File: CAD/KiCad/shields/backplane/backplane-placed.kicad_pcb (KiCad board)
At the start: 2 copper layers, 210 x 297 mm, 103 parts, among them J1 DSUB-15, J2 DC jack, J5 DSUB-15, J6 screw bridge, J7 JST EH 3, M1 U2D2

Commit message: Route the shield set and validate shared interfaces
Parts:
- added HM1: M3 computing shield, Shields:MountingHole_3.2mm_M3, F.Cu at (143.7, 149.8)
- added HM2: M3 computing shield, Shields:MountingHole_3.2mm_M3, F.Cu at (192.0, 68.6)
- added HM3: M3 computing shield, Shields:MountingHole_3.2mm_M3, F.Cu at (192.0, 143.5)
- added HM4: M3 computing shield, Shields:MountingHole_3.2mm_M3, F.Cu at (143.7, 67.3)

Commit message: Remove shield identification and adopt the simplified connector and Teensy pin maps
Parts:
- removed CI1: 10uF X7R, Shields:C_0805_2012Metric
- removed H1, H2, H3, H4: M3 3.2mm NPTH, Colloquy:MountingHole_3.2mm_M3
- removed RI1, RI2: 4K7, Shields:R_0603_1608Metric
- removed TPI2: shield/sda, Shields:TestPoint_Pad_D1.5mm
- removed TPI3: shield/scl, Shields:TestPoint_Pad_D1.5mm
- added TPA1: female1/analyser out, Shields:TestPoint_Pad_D1.5mm, F.Cu at (100.0, 305.0)
- added TPA2: female2/analyser out, Shields:TestPoint_Pad_D1.5mm, F.Cu at (122.0, 305.0)
- added TPA3: female3/analyser out, Shields:TestPoint_Pad_D1.5mm, F.Cu at (144.0, 305.0)
- added TPA4: male1/analyser out, Shields:TestPoint_Pad_D1.5mm, F.Cu at (166.0, 305.0)
- added TPA5: male2/analyser out, Shields:TestPoint_Pad_D1.5mm, F.Cu at (188.0, 305.0)
- added TPL1: female1/filter out, Shields:TestPoint_Pad_D1.5mm, F.Cu at (90.0, 225.0)
- added TPL2: female2/filter out, Shields:TestPoint_Pad_D1.5mm, F.Cu at (122.0, 225.0)
- added TPL3: female3/filter out, Shields:TestPoint_Pad_D1.5mm, F.Cu at (154.0, 225.0)
- added TPL4: male1/filter out, Shields:TestPoint_Pad_D1.5mm, F.Cu at (186.0, 225.0)
- added TPL5: male2/filter out, Shields:TestPoint_Pad_D1.5mm, F.Cu at (218.0, 225.0)
- added TPM1: female1/microphone, Shields:TestPoint_Pad_D1.5mm, F.Cu at (100.0, 283.0)
- added TPM2: female2/microphone, Shields:TestPoint_Pad_D1.5mm, F.Cu at (122.0, 283.0)
- added TPM3: female3/microphone, Shields:TestPoint_Pad_D1.5mm, F.Cu at (144.0, 283.0)
- added TPM4: male1/microphone, Shields:TestPoint_Pad_D1.5mm, F.Cu at (166.0, 283.0)
- added TPM5: male2/microphone, Shields:TestPoint_Pad_D1.5mm, F.Cu at (188.0, 283.0)
- JA1: value ANALYSER - KEY 24 -> ANALYSER - KEY 22; footprint Shields:Header_2x12_Key24 -> Shields:Header_2x11_Key22
- JV1: value female1 - KEY 14 -> female1 - KEY 6; footprint Shields:Header_2x07_Key14 -> Shields:Header_2x03_Key6
- JV2: value female2 - KEY 14 -> female2 - KEY 6; footprint Shields:Header_2x07_Key14 -> Shields:Header_2x03_Key6
- JV3: value female3 - KEY 14 -> female3 - KEY 6; footprint Shields:Header_2x07_Key14 -> Shields:Header_2x03_Key6
- JV4: value male1 - KEY 14 -> male1 - KEY 6; footprint Shields:Header_2x07_Key14 -> Shields:Header_2x03_Key6
- JV5: value male2 - KEY 14 -> male2 - KEY 6; footprint Shields:Header_2x07_Key14 -> Shields:Header_2x03_Key6
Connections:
- A1 pad SCL: shield/scl -> (no net)
- A1 pad SDA: shield/sda -> (no net)
- JA1 pad 19: shield/sda -> IOREF
- JA1 pad 20: shield/scl -> GND
- JA1 pad 21: IOREF -> +5V

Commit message: Route microphones directly to Teensy and remove the analyser buffer board
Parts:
- removed TPI1: IOREF, Shields:TestPoint_Pad_D1.5mm
- added RM1: 4K7, Shields:R_0603_1608Metric, F.Cu at (100.0, 289.0)
- added RM2: 4K7, Shields:R_0603_1608Metric, F.Cu at (122.0, 289.0)
- added RM3: 4K7, Shields:R_0603_1608Metric, F.Cu at (144.0, 289.0)
- added RM4: 4K7, Shields:R_0603_1608Metric, F.Cu at (166.0, 289.0)
- added RM5: 4K7, Shields:R_0603_1608Metric, F.Cu at (184.0, 289.0)
- added RMD1: 1M, Shields:R_0603_1608Metric, F.Cu at (104.0, 292.0)
- added RMD2: 1M, Shields:R_0603_1608Metric, F.Cu at (126.0, 292.0)
- added RMD3: 1M, Shields:R_0603_1608Metric, F.Cu at (148.0, 292.0)
- added RMD4: 1M, Shields:R_0603_1608Metric, F.Cu at (170.0, 292.0)
- added RMD5: 1M, Shields:R_0603_1608Metric, F.Cu at (184.0, 293.0)
- added TPD1: female1/mic direct, Shields:TestPoint_Pad_D1.5mm, F.Cu at (100.0, 296.0)
- added TPD2: female2/mic direct, Shields:TestPoint_Pad_D1.5mm, F.Cu at (122.0, 296.0)
- added TPD3: female3/mic direct, Shields:TestPoint_Pad_D1.5mm, F.Cu at (144.0, 296.0)
- added TPD4: male1/mic direct, Shields:TestPoint_Pad_D1.5mm, F.Cu at (166.0, 296.0)
- added TPD5: male2/mic direct, Shields:TestPoint_Pad_D1.5mm, F.Cu at (184.0, 298.0)
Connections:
- A1 pad D26: (no net) -> female1/mic direct
- A1 pad D27: (no net) -> female2/mic direct
- A1 pad D28: (no net) -> female3/mic direct
- A1 pad D29: (no net) -> male1/mic direct
- A1 pad D30: (no net) -> male2/mic direct
- A1 pad IORF: IOREF -> (no net)
- JA1 pad 19: IOREF -> MEGA_5V
- JA1 pad 21: +5V -> GND
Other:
- copper layers 2 -> 4
- board text added: "1"
- board text added: "1 ANA"
- board text added: "1 LINE"
- board text added: "2 ANA"
- board text added: "2 LINE"
- board text added: "3 ANA"
- board text added: "3 LINE"
- board text added: "4 ANA"
- board text added: "4 LINE"
- board text added: "5 ANA"
- board text added: "5 LINE"
- board text added: "AGND"
- board text added: "AMP SHUTDOWN"
- board text added: "ANA 1"
- board text added: "ANA 2"
- board text added: "ANA 3"
- board text added: "ANA 4"
- board text added: "ANA 5"
- board text added: "AUDIO RTN"
- board text added: "BOARD +5V"
- board text added: "CARD PITCH Hz"
- board text added: "CHANGE A SHIELD ONLY WITH BOTH UNPLUGGED"
- board text added: "COLLOQUY - SHIELD BACKPLANE - REV A"
- board text added: "COMPUTING SLOT MEGA 2560 OR TEENSY ADAPTER"
- board text added: "GND"
- board text added: "JA1 - MSGEQ7 ANALYSER - MEGA ONLY - EMPTY WITH TEENSY"
- board text added: "JP1 - ONLY AGND-GND BOND"
- board text added: "JV1 - FEMALE1 MEGA D6 - TEENSY 2"
- board text added: "JV2 - FEMALE2 MEGA D46 - TEENSY 4"
- board text added: "JV3 - FEMALE3 MEGA D10 - TEENSY 5"
- board text added: "JV4 - MALE1 MEGA D11 - TEENSY 6"
- board text added: "JV5 - MALE2 MEGA D5 - TEENSY 28"
- board text added: "KEY <-"
- board text added: "LINE 1"
- board text added: "LINE 2"
- board text added: "LINE 3"
- board text added: "LINE 4"
- board text added: "LINE 5"
- board text added: "LINE OUT"
- board text added: "M3"
- board text added: "MEGA 5V (COMPUTING USB)"
- board text added: "MIC 1"
- board text added: "MIC 2"
- board text added: "MIC 3"
- board text added: "MIC 4"
- board text added: "MIC 5"
- board text added: "MIC DIRECT - 4.7 K - TO TEENSY A0-A4"
- board text added: "MIC DIRECT 1"
- board text added: "MIC DIRECT 2"
- board text added: "MIC DIRECT 3"
- board text added: "MIC DIRECT 4"
- board text added: "MIC DIRECT 5"
- board text added: "MIC ORDER F1 F2 F3 M1 M2 - MODULE N = BODY N"
- board text added: "POWER RACK AND COMPUTING USB TOGETHER"
- board text added: "RESET"
- board text added: "SERVO BUS - 12 V"
- board text added: "SLOT N = BODY N"
- board text added: "STROBE"
- board text added: "TONE 1"
- board text added: "TONE 2"
- board text added: "TONE 3"
- board text added: "TONE 4"
- board text added: "TONE 5"
- board text added: "U2D2"
- board text added: "USB END ^"
- board text removed: "COLLOQUY / SHIELDS / A"
- board text removed: "IOREF: MEGA 5V / TEENSY 3.3V"
- board text removed: "JV1 female1"
- board text removed: "JV2 female2"
- board text removed: "JV3 female3"
- board text removed: "JV4 male1"
- board text removed: "JV5 male2"

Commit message: Update shields for Thomas RC cards, debug headers and body microphones
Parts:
- removed TP11, TP12, TP13, TP14, TP15: test pad, Shields:TestPoint_Pad_D1.5mm
- added DP12: GREEN LED, Shields:LED_0603_1608Metric, F.Cu at (217.0, 84.0)
- added DP5: GREEN LED, Shields:LED_0603_1608Metric, F.Cu at (210.0, 84.0)
- added DPUSB: GREEN LED, Shields:LED_0603_1608Metric, F.Cu at (224.0, 84.0)
- added DT1: YELLOW LED, Shields:LED_0603_1608Metric, F.Cu at (82.5, 194.0)
- added DT2: YELLOW LED, Shields:LED_0603_1608Metric, F.Cu at (113.0, 194.0)
- added DT3: YELLOW LED, Shields:LED_0603_1608Metric, F.Cu at (143.5, 194.0)
- added DT4: YELLOW LED, Shields:LED_0603_1608Metric, F.Cu at (174.0, 194.0)
- added DT5: YELLOW LED, Shields:LED_0603_1608Metric, F.Cu at (204.5, 194.0)
- added RLP12: 4K7, Shields:R_0603_1608Metric, F.Cu at (217.0, 87.0)
- added RLP5: 2K2, Shields:R_0603_1608Metric, F.Cu at (210.0, 87.0)
- added RLPUSB: 2K2, Shields:R_0603_1608Metric, F.Cu at (224.0, 87.0)
- added RLT1: 1K5, Shields:R_0603_1608Metric, F.Cu at (82.5, 197.0)
- added RLT2: 1K5, Shields:R_0603_1608Metric, F.Cu at (113.0, 197.0)
- added RLT3: 1K5, Shields:R_0603_1608Metric, F.Cu at (143.5, 197.0)
- added RLT4: 1K5, Shields:R_0603_1608Metric, F.Cu at (174.0, 197.0)
- added RLT5: 1K5, Shields:R_0603_1608Metric, F.Cu at (204.5, 197.0)
- added TPEG: AGND, Shields:TestPin_1x01_P2.54mm, F.Cu at (151.6, 322.0)
- added TPUSB: MEGA_5V, Shields:TestPin_1x01_P2.54mm, F.Cu at (221.2, 93.0)
- added TPVG: AGND, Shields:TestPin_1x01_P2.54mm, F.Cu at (222.2, 202.0)
- TP1: value test pad -> male1/filter out
- TP2: value test pad -> male2/filter out
- TP20: value test pad -> analyser/strobe
- TP21: value test pad -> analyser/reset
- TP3: value test pad -> female1/filter out
- TP30: value test pad -> amp shutdown
- TP31: value test pad -> +5V; footprint Shields:TestPoint_Pad_D1.5mm -> Shields:TestPin_1x01_P2.54mm
- TP32: value test pad -> MEGA_5V
- TP33: value test pad -> +12V; footprint Shields:TestPoint_Pad_D1.5mm -> Shields:TestPin_1x01_P2.54mm
- TP34: value test pad -> GND; footprint Shields:TestPoint_Pad_D1.5mm -> Shields:TestPin_1x01_P2.54mm
- TP4: value test pad -> female2/filter out
- TP5: value test pad -> female3/filter out
- TPA1, TPA2, TPA3, TPA4, TPA5, TPD1, TPD2, TPD3, TPD4, TPD5, TPL1, TPL2, TPL3, TPL4, TPL5, TPV1, TPV2, TPV3, TPV4, TPV5: footprint Shields:TestPoint_Pad_D1.5mm -> Shields:TestPin_1x01_P2.54mm
- moved TP34 116.8 mm to (223.7, 93.0)
- moved TPD5 51.1 mm to (138.9, 322.0)
- moved TPA5 49.5 mm to (141.5, 322.0)
- moved TPD4 45.4 mm to (128.8, 322.0)
- moved TPM5 39.5 mm to (160.2, 311.1)
- moved TPA4 38.6 mm to (131.3, 322.0)
- moved TPD3 36.3 mm to (118.6, 322.0)
- moved TPD2 29.3 mm to (108.5, 322.0)
- moved TPA3 28.5 mm to (121.2, 322.0)
- moved TPD1 26.1 mm to (98.3, 322.0)
- moved TPL5 25.5 mm to (207.0, 202.0)
- moved TPL4 24.9 mm to (176.5, 202.0)
- moved TPL3 24.3 mm to (146.0, 202.0)
- moved TPL2 23.9 mm to (115.6, 202.0)
- moved TPL1 23.5 mm to (85.1, 202.0)
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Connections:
- TP33 pad 1: GND -> +12V
- TP34 pad 1: AGND -> GND
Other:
- board text added: "12V"
- board text added: "5V"
- board text added: "A1"
- board text added: "A2"
- board text added: "A3"
- board text added: "A4"
- board text added: "A5"
- board text added: "BOARD 5V"
- board text added: "L1"
- board text added: "L2"
- board text added: "L3"
- board text added: "L4"
- board text added: "L5"
- board text added: "M1"
- board text added: "M2"
- board text added: "M4"
- board text added: "M5"
- board text added: "MEGA 5V"
- board text added: "T = TONE / L = LINE"
- board text added: "T1"
- board text added: "T2"
- board text added: "T3"
- board text added: "T4"
- board text added: "T5"
- board text added: "USB"
- board text removed: "1 ANA"
- board text removed: "2 ANA"
- board text removed: "3 ANA"
- board text removed: "4 ANA"
- board text removed: "5 ANA"
- board text removed: "ANA 1"
- board text removed: "ANA 2"
- board text removed: "ANA 3"
- board text removed: "ANA 4"
- board text removed: "ANA 5"
- board text removed: "BOARD +5V"
- board text removed: "LINE 1"
- board text removed: "LINE 2"
- board text removed: "LINE 3"
- board text removed: "LINE 4"
- board text removed: "LINE 5"
- board text removed: "MIC DIRECT 1"
- board text removed: "MIC DIRECT 2"
- board text removed: "MIC DIRECT 3"
- board text removed: "MIC DIRECT 4"
- board text removed: "MIC DIRECT 5"
- board text removed: "SLOT N = BODY N"

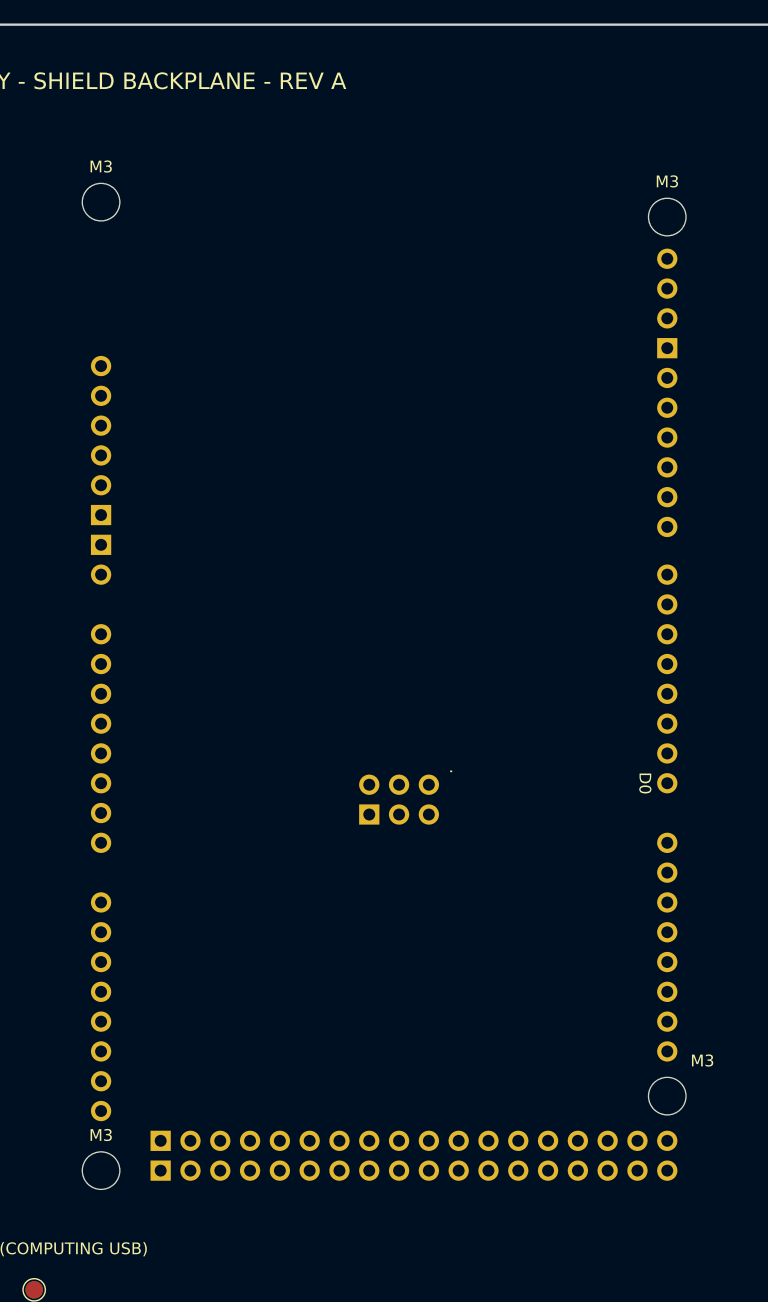
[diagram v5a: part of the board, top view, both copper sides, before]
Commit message: Move the computing slot to the front and widen outer servo power routing
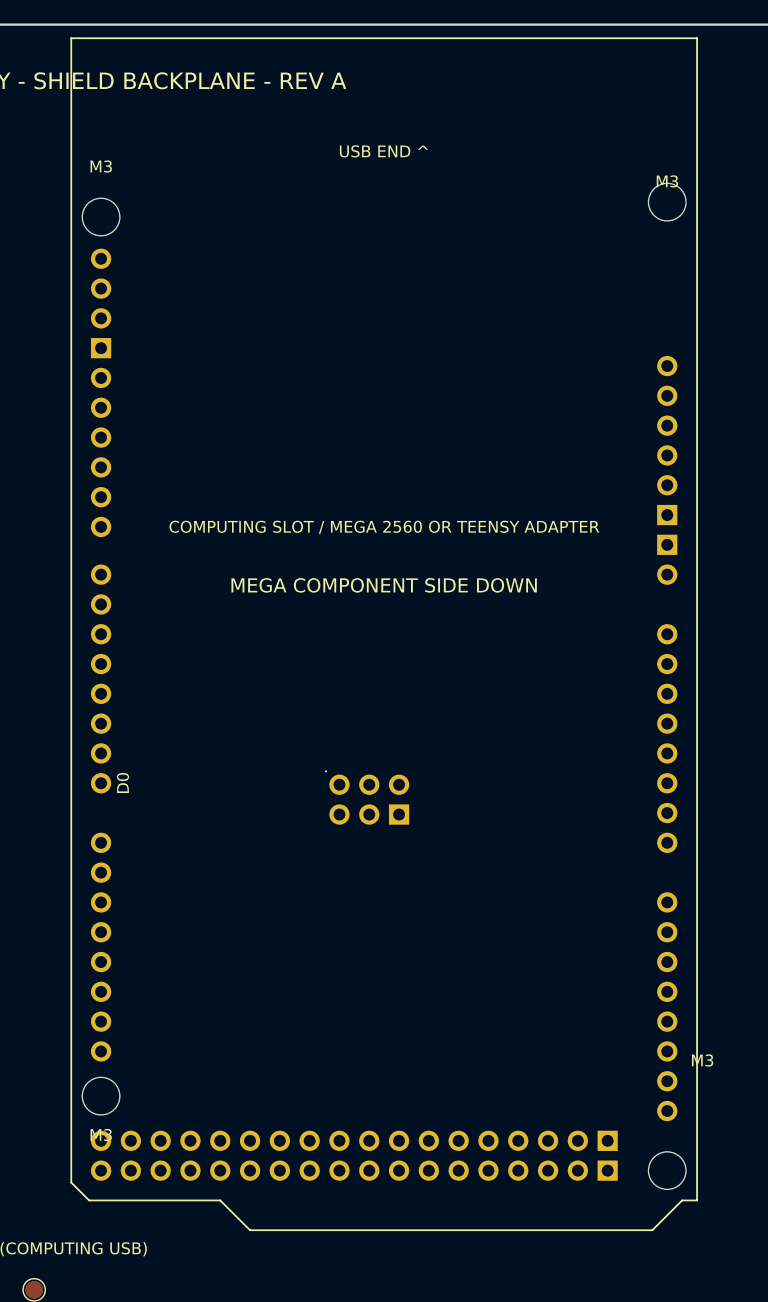
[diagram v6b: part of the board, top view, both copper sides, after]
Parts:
- A1: footprint Shields:Arduino_Mega2560_R3_Shield -> Shields:Mega_Front_Mirrored
- HM1, HM2, HM3, HM4: value M3 computing shield -> M3; front spacer OD <=4mm; screw head on rear; footprint Shields:MountingHole_3.2mm_M3 -> Shields:MountingHole_3.2mm_M3_SlimFront
- moved A1 53.3 mm to (194.5, 53.3)
- moved HM1 48.3 mm to (192.0, 149.8)
- moved HM2 48.3 mm to (143.7, 68.6)
- moved HM3 48.3 mm to (143.7, 143.5)
- moved HM4 48.3 mm to (192.0, 67.3)
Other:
- board text added: "COMPUTING SLOT / MEGA 2560 OR TEENSY ADAPTER"
- board text added: "MEGA COMPONENT SIDE DOWN"
- board text removed: "COMPUTING SLOT MEGA 2560 OR TEENSY ADAPTER"

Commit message: Restore the original enclosure holes in the backplane
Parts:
- moved TPL3 6.43 mm to (141.0, 206.0)
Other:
- outline, holes or cut-outs redrawn
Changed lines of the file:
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@@
 	(footprint "Shields:TestPin_1x01_P2.54mm"
 		(layer "F.Cu")
-		(at 146.04 202)
+		(at 141 206)
 		(descr "Through hole straight pin header, 1x01, 2.54mm pitch, single row")
 		(tags "Through hole pin header THT 1x01 2.54mm single row")
@@
 		(layer "Edge.Cuts")
 	)
+	(gr_circle
+		(center 149 72.16)
+		(end 153 72.16)
+		(stroke
+			(width 0.1)
+			(type default)
+		)
+		(fill no)
+		(layer "Edge.Cuts")
+	)
+	(gr_circle
+		(center 234 202.16)
+		(end 238 202.16)
+		(stroke
+			(width 0.1)
+			(type default)
+		)
+		(fill no)
+		(layer "Edge.Cuts")
+	)
 	(gr_arc
 		(start 254 344.16)
@@
 		(layer "Edge.Cuts")
 	)
+	(gr_circle
+		(center 64 202.16)
+		(end 68 202.16)
+		(stroke
+			(width 0.1)
+			(type default)
+		)
+		(fill no)
+		(layer "Edge.Cuts")
+	)
 	(gr_line
 		(start 49 349.16)
@@
 		(layer "Edge.Cuts")
 	)
+	(gr_circle
+		(center 149 202.16)
+		(end 153 202.16)
+		(stroke
+			(width 0.1)
+			(type default)
+		)
+		(fill no)
+		(layer "Edge.Cuts")
+	)
 	(gr_text "USB"
 		(at 221.16 89.5 0)
@@
 	)
 	(gr_text "T = TONE / L = LINE"
-		(at 151 199 0)
+		(at 145 187.8 0)
 		(layer "F.SilkS")
 		(effects
@@
 	)
 	(gr_text "L3"
-		(at 146.04 205.5 0)
+		(at 141 209.5 0)
 		(layer "F.SilkS")
 		(effects
